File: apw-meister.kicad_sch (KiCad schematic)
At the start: 48 parts, among them J1 USB4105-GF-A-120, J2 APW12 PSU Comm, Q1 DMG1012T-7, SW2 B3U-1000P, SW3 B3U-1000P, U1 SK6812SIDE-A-RVS, U3 RP2354A, U4 AP2112K-3.3TRG1, U5 TPD6E05U06RVZR, U6 TPD4E05U06DQAR, Y1 12MHz

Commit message: Checkpoint RP2354A schematic, models, and initial PCB routing
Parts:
- C10, C11, C12, C13, C14, C15, C16, C17, C18, C19, C2, C20, C21, C22, C23, C24, C4, C6, C7, C8, C9: footprint Capacitor_SMD:C_0402_1005Metric -> aditBoard:C_0402_1005Metric
- Q1: footprint Package_TO_SOT_SMD:SOT-523 -> aditBoard:SOT-523
- R10, R11, R12, R13, R14, R2, R3, R4, R5, R6, R7, R8, R9: footprint Resistor_SMD:R_0402_1005Metric -> aditBoard:R_0402_1005Metric
- SW2: footprint Button_Switch_SMD:SW_SPST_B3U-1000P -> aditBoard:SW_SPST_B3U-1000P
- SW3: footprint Button_Switch_SMD:SW_SPST_B3U-1000P -> aditBoard:SW_SPST_B3U-1000P; now not fitted
- U5: footprint Package_SON:Texas_R-PUSON-N14 -> aditBoard:Texas_R-PUSON-N14
- U6: footprint Package_SON:USON-10_2.5x1.0mm_P0.5mm -> aditBoard:USON-10_2.5x1.0mm_P0.5mm
- Y1: footprint Crystal:Crystal_SMD_3225-4Pin_3.2x2.5mm -> aditBoard:Crystal_SMD_3225-4Pin_3.2x2.5mm

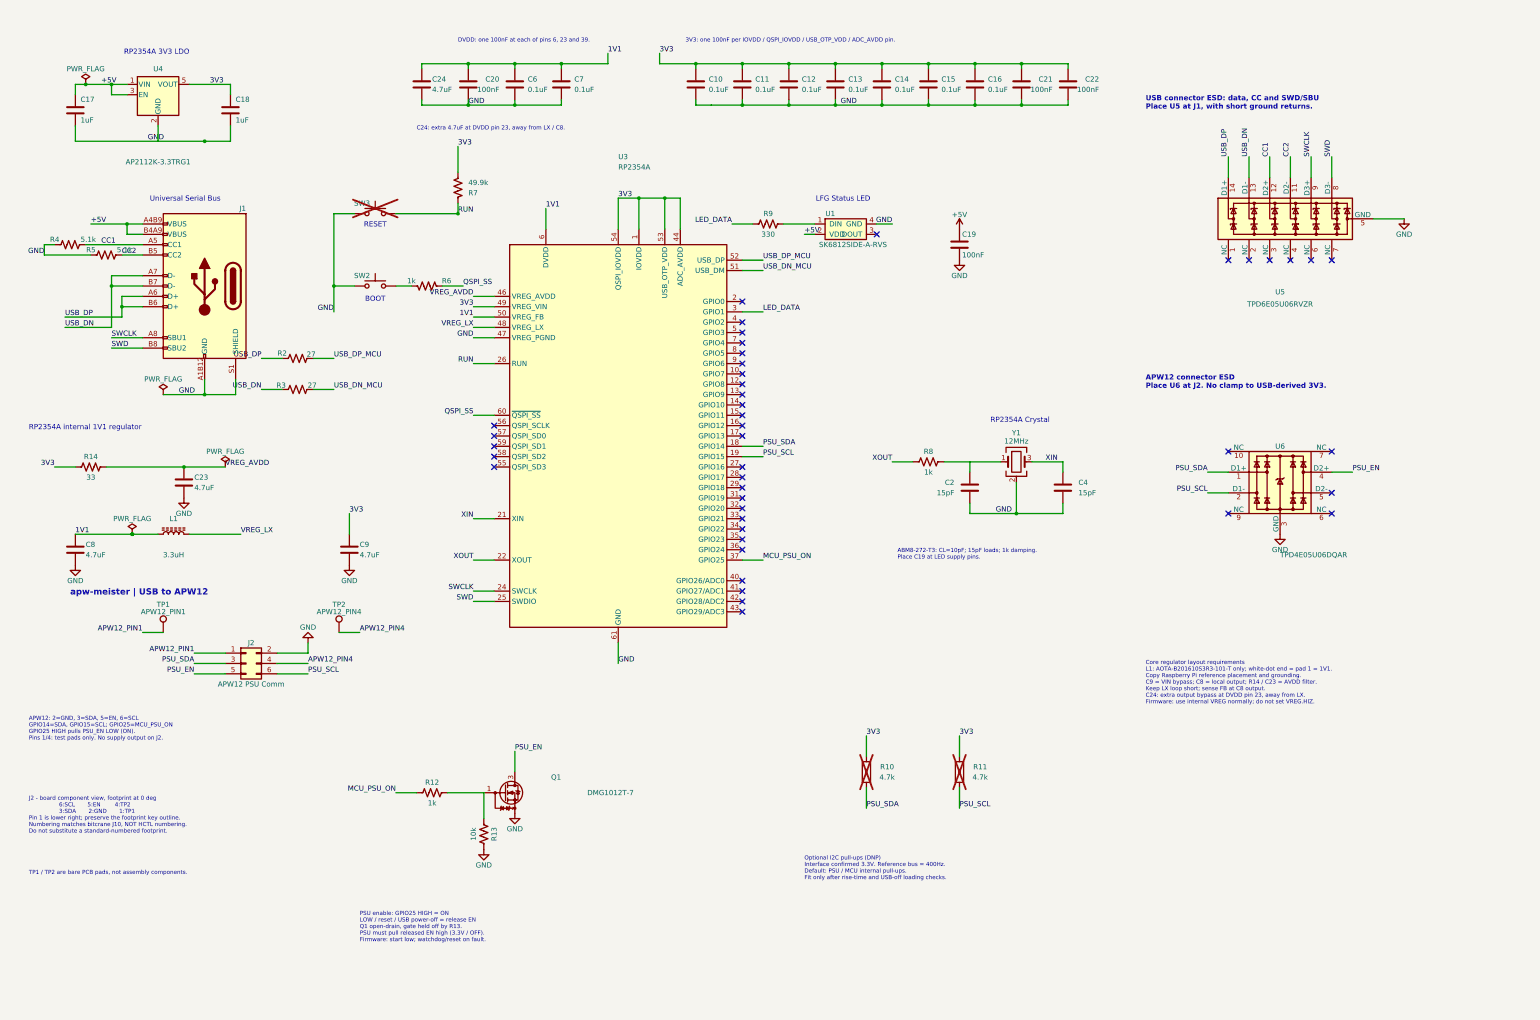
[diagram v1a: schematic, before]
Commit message: Migrate apw-meister hardware to CH32X035F8U6
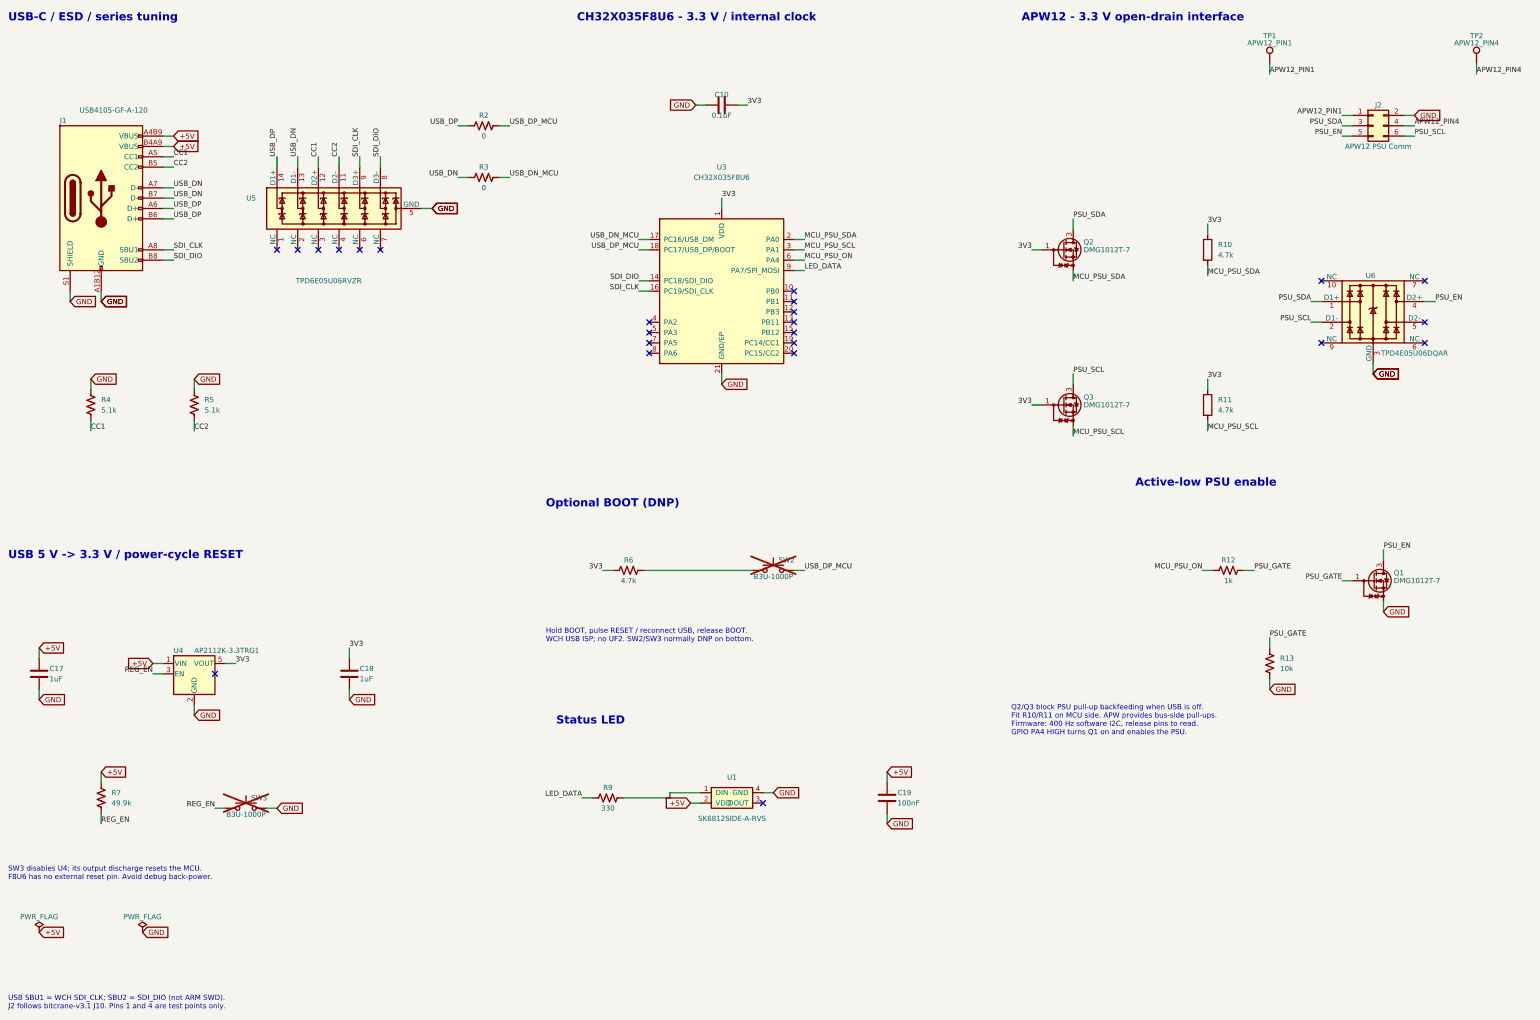
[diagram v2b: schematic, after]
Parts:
- removed C11, C12, C13, C14, C15, C16, C6, C7: 0.1uF, aditBoard:C_0402_1005Metric, symbol Device:C
- removed C2, C4: 15pF, aditBoard:C_0402_1005Metric, symbol Device:C
- removed C20, C21, C22: 100nF, aditBoard:C_0402_1005Metric, symbol Device:C
- removed C23, C24, C8, C9: 4.7uF, aditBoard:C_0402_1005Metric, symbol Device:C
- removed L1: 3.3uH, aditBoard:L_Abracon_AOTA-B201610S3R3-101-T, symbol Device:L_Ferrite
- removed R14: 33, aditBoard:R_0402_1005Metric, symbol Device:R_US
- removed R8: 1k, aditBoard:R_0402_1005Metric, symbol Device:R_US
- removed U3: RP2354A, aditBoard:QFN-60-1EP_7x7mm_P0.4mm_EP3.4x3.4mm, symbol rp2354:RP2354A
- removed Y1: 12MHz, aditBoard:Crystal_SMD_3225-4Pin_3.2x2.5mm, symbol Device:Crystal_GND24
- added Q2, Q3: DMG1012T-7, aditBoard:SOT-523, symbol Transistor_FET:DMG1012T
- added U3: CH32X035F8U6, aditBoard:VQFN-20-1EP_3x3mm_P0.4mm_EP1.7x1.7mm, symbol wch32:CH32X035F8U6
- R10, R11: Assembly note DNP by default; validate rise time and USB-off loading befo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 -> FIT: MCU-side 4.7k pull-up; APW side uses PSU pull-ups.; now fitted
- R2, R3: value 27 -> 0; Assembly note (none) -> USB series tuning position; fit 0 ohm for WCH reference cir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; JLC Part Extended Part -> Basic Part; JLCPCB Part # C25100 -> C17168; LCSC C25100 -> C17168; MPN 0402WGF270JTCE -> 0402WGF0000TCE; PARTNO 0402WGF270JTCE -> 0402WGF0000TCE
- R6: value 1k -> 4.7k; Assembly note (none) -> BOOT pull-up to 3.3 V through optional SW2.; JLC Part Extended Part -> Basic Part; JLCPCB Part # C106235 -> C25900; LCSC C106235 -> C25900; MPN RC0402FR-071KL -> 0402WGF4701TCE; Manufacturer YAGEO -> UNI-ROYAL(Uniroyal Elec); PARTNO RC0402FR-071KL -> 0402WGF4701TCE
- SW2: Assembly note (none) -> DNP: optional bottom-side development button.; now not fitted
- SW3: Assembly note (none) -> DNP: optional bottom-side development button.
- TP1, TP2: footprint TestPoint:TestPoint_Pad_D1.0mm -> aditBoard:TestPoint_Pad_D1.0mm; now in the parts list
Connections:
- net QSPI_SS is gone; now on net 3V3: R6.1
- net +5V: now also R7.1; no longer U4.3 (EN)
- net 3V3: now also Q2.1 (G), Q3.1 (G), U3.1 (VDD); no longer R7.2
- net GND: now also U3.21 (GND/EP); no longer SW2.2
- net LED_DATA: now also U3.9 (PA7/SPI_MOSI)
- net MCU_PSU_ON: now also U3.6 (PA4)
- net PSU_SCL: now also Q3.3 (D); no longer R11.2
- net PSU_SDA: now also Q2.3 (D); no longer R10.2
- net USB_DN_MCU: now also U3.17 (PC16/USB_DM)
- net USB_DP_MCU: now also SW2.2, U3.18 (PC17/USB_DP/BOOT)
- net PSU_GATE: now reaches Q1.1 (G), R12.2, R13.1
- net RUN renamed REG_EN
- net REG_EN: now also R7.2, U4.3 (EN); no longer R7.1
- net SWCLK renamed SDI_CLK
- net SDI_CLK: now also U3.16 (PC19/SDI_CLK)
- net SWD renamed SDI_DIO
- net SDI_DIO: now also U3.14 (PC18/SDI_DIO)
- new net MCU_PSU_SCL: Q3.2 (S), R11.2, U3.3 (PA1)
- new net MCU_PSU_SDA: Q2.2 (S), R10.2, U3.2 (PA0)
- no-connect marks 43 -> 24
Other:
- note added: "APW12 - 3.3 V open-drain interface"
- note added: "Active-low PSU enable"
- note added: "CH32X035F8U6 - 3.3 V / internal clock"
- note added: "Hold BOOT, pulse RESET / reconnect USB, release BOOT. WCH USB ISP; no UF2. SW2/SW3 normally DNP on bottom."
- note added: "Optional BOOT (DNP)"
- note added: "Q2/Q3 block PSU pull-up backfeeding when USB is off. Fit R10/R11 on MCU side. APW provides bus-side pull-ups. Firmware: 400 Hz software I2C, release pins to read. GPIO PA4 HIGH turns Q1 on and enables the PSU."
- note added: "SW3 disables U4; its output discharge resets the MCU. F8U6 has no external reset pin. Avoid debug back-power."
- note added: "Status LED"
- note added: "USB 5 V -> 3.3 V / power-cycle RESET"
- note added: "USB SBU1 = WCH SDI_CLK; SBU2 = SDI_DIO (not ARM SWD). J2 follows bitcrane-v3.1 J10. Pins 1 and 4 are test points only."
- note added: "USB-C / ESD / series tuning"
- note removed: "3V3: one 100nF per IOVDD / QSPI_IOVDD / USB_OTP_VDD / ADC_AVDD pin."
- note removed: "ABM8-272-T3: CL=10pF; 15pF loads; 1k damping. Place C19 at LED supply pins."
- note removed: "APW12 connector ESD Place U6 at J2. No clamp to USB-derived 3V3."
- note removed: "APW12: 2=GND, 3=SDA, 5=EN, 6=SCL GPIO14=SDA, GPIO15=SCL; GPIO25=MCU_PSU_ON GPIO25 HIGH pulls PSU_EN LOW (ON). Pins 1/4: test pads only. No supply output on J2."
- note removed: "BOOT"
- note removed: "C24: extra 4.7uF at DVDD pin 23, away from LX / C8."
- note removed: "Core regulator layout requirements L1: AOTA-B201610S3R3-101-T only; white-dot end = pad 1 = 1V1. Copy Raspberry Pi reference placement and grounding. C9 = VIN bypass; C8 = local output; R14 / C23 = AVDD filter. Keep LX loop short; sense FB at C8 output. C24: extra output bypass at DVDD pin 23, away from LX. Firmware: use internal VREG normally; do not set VREG.HIZ."
- note removed: "DVDD: one 100nF at each of pins 6, 23 and 39."
- note removed: "J2 - board component view, footprint at 0 deg 6:SCL 5:EN 4:TP2 3:SDA 2:GND 1:TP1 Pin 1 is lower right; preserve the footprint key outline. Numbering matches bitcrane J10, NOT HCTL numbering. Do not substitute a standard-numbered footprint."
- note removed: "LFG Status LED"
- note removed: "Optional I2C pull-ups (DNP) Interface confirmed 3.3V. Reference bus = 400Hz. Default: PSU / MCU internal pull-ups. Fit only after rise-time and USB-off loading checks."
- note removed: "PSU enable: GPIO25 HIGH = ON LOW / reset / USB power-off = release EN Q1 open-drain, gate held off by R13. PSU must pull released EN high (3.3V / OFF). Firmware: start low; watchdog/reset on fault."
- note removed: "RESET"
- note removed: "RP2354A 3V3 LDO"
- note removed: "RP2354A Crystal"
- note removed: "RP2354A internal 1V1 regulator"
- note removed: "TP1 / TP2 are bare PCB pads, not assembly components."
- note removed: "USB connector ESD: data, CC and SWD/SBU Place U5 at J1, with short ground returns."
- note removed: "Universal Serial Bus"
- note removed: "apw-meister | USB to APW12"
- title: apw-meister -> apw-meister - CH32X035F8U6
